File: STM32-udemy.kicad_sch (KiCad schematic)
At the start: 23 parts, among them J1 USB_B_Micro, J2 Serial_Wire, J3 Conn_01x20_Male, J4 Conn_01x20_Male, SW1 SW_Push, SW2 SW_SPDT, U1 STM32F446RCTx, Y1 Crystal_GND24

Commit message: Schematic and basic layout
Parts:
- removed C7: 100n, symbol Device:C
- added C1, C2: 10u, Capacitor_SMD:C_0805_2012Metric_Pad1.18x1.45mm_HandSolder, symbol Device:C
- added D1: PWR_LED, LED_SMD:LED_0603_1608Metric_Pad1.05x0.95mm_HandSolder, symbol Device:LED
- added H1: MountingHole, MountingHole:MountingHole_2.2mm_M2_ISO7380_Pad, symbol Mechanical:MountingHole_Pad
- added H2, H3, H4: MountingHole, MountingHole:MountingHole_2.2mm_M2_Pad, symbol Mechanical:MountingHole_Pad
- added R2: 10k, Resistor_SMD:R_0603_1608Metric_Pad0.98x0.95mm_HandSolder, symbol Device:R
- added U1: NCP1117, Package_TO_SOT_SMD:SOT-223-3_TabPin2, symbol Regulator_Linear:NCP1117-3.3_SOT223
- C10: renamed from C9; footprint (none) -> Capacitor_SMD:C_0603_1608Metric_Pad1.08x0.95mm_HandSolder
- C11: renamed from C10; footprint (none) -> Capacitor_SMD:C_0603_1608Metric_Pad1.08x0.95mm_HandSolder
- C12: renamed from C11; footprint (none) -> Capacitor_SMD:C_0603_1608Metric_Pad1.08x0.95mm_HandSolder
- C13: renamed from C12; footprint (none) -> Capacitor_SMD:C_0402_1005Metric_Pad0.74x0.62mm_HandSolder
- C14: renamed from C13; footprint (none) -> Capacitor_SMD:C_0402_1005Metric_Pad0.74x0.62mm_HandSolder
- C3: renamed from C1; footprint (none) -> Capacitor_SMD:C_0805_2012Metric_Pad1.18x1.45mm_HandSolder
- C4: renamed from C2; footprint (none) -> Capacitor_SMD:C_0603_1608Metric_Pad1.08x0.95mm_HandSolder
- C5: renamed from C3; footprint (none) -> Capacitor_SMD:C_0603_1608Metric_Pad1.08x0.95mm_HandSolder
- C6: renamed from C4; footprint (none) -> Capacitor_SMD:C_0603_1608Metric_Pad1.08x0.95mm_HandSolder
- C7: renamed from C5; footprint (none) -> Capacitor_SMD:C_0603_1608Metric_Pad1.08x0.95mm_HandSolder
- C8: renamed from C6; footprint (none) -> Capacitor_SMD:C_0603_1608Metric_Pad1.08x0.95mm_HandSolder
- C9: renamed from C8; footprint (none) -> Capacitor_SMD:C_0603_1608Metric_Pad1.08x0.95mm_HandSolder
- FB1: footprint (none) -> Inductor_SMD:L_0603_1608Metric_Pad1.05x0.95mm_HandSolder
- J1: footprint (none) -> Connector_USB:USB_Micro-B_Wuerth_629105150521
- J2: footprint (none) -> Connector_PinHeader_2.54mm:PinHeader_1x04_P2.54mm_Vertical
- J3, J4: footprint (none) -> Connector_PinHeader_2.54mm:PinHeader_1x20_P2.54mm_Vertical
- R1: value 10k -> 1K; footprint (none) -> Resistor_SMD:R_0603_1608Metric_Pad0.98x0.95mm_HandSolder
- SW1: footprint (none) -> Button_Switch_SMD:SW_Push_1P1T_NO_Vertical_Wuerth_434133025816
- SW2: footprint (none) -> Button_Switch_SMD:SW_SPDT_PCM12
- Y1: footprint (none) -> Crystal:Crystal_SMD_3225-4Pin_3.2x2.5mm
- renumbered U1 to U2
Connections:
- net +3V3: now also J2.1 (Pin_1), C2.1, D1.2 (A), U1.2 (VO); no longer J2.4 (Pin_4)
- net BOOT0: now also R2.1; no longer R1.1
- net GND: now also R1.2, C1.2, C2.2, H1.1, H2.1, H3.1, H4.1, U1.1 (GND)
- net SWCLK: now also J2.4 (Pin_4); no longer J2.3 (Pin_3)
- net SWDIO: now also J2.3 (Pin_3); no longer J2.1 (Pin_1)
- net SW_BOOT0: now also R2.2; no longer R1.2
- net VBUS: now also C1.1, U1.3 (VI); no longer U2.42 (PA9)
- net HSE_IN: now reaches C13.1, U2.5 (PH0), Y1.1
- net HSE_OUT: now reaches C14.1, U2.6 (PH1), Y1.3
- net PC0: no longer names the net of U2.8 (PC0)
- net PC1: no longer names the net of U2.9 (PC1)
- net PC2: no longer names the net of U2.10 (PC2)
- net PC3: no longer names the net of U2.11 (PC3)
- net USB_ID: no longer names the net of U2.43 (PA10)
- net USB_ID: no longer J1.4 (ID)
- new net PWR_LED: D1.1 (K), R1.1
- no-connect marks 2 -> 7
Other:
- note added: "Analog Supply filtering"
- note added: "BOOT selector switch"
- note added: "Connectors"
- note added: "Crystal oscillator circuitry"
- note added: "Decoupling capacitors"
- note added: "LED to indicate when the board is powered ON"
- note added: "Linear voltage regulator to power the board from the USB (nominal 5V)"
- note added: "Microcontroller circuitry"
- note added: "Mounting Holes"
- note added: "One 10uF Cap for the whole IC and one 100nF Cap for each VDD/VBAT pin - AN4488"
- note added: "Power LED"
- note added: "Power Supply"
- note added: "Reset Button"
- note added: "SIZE: M2"
- note added: "Serial Wire Debbuger/Programmer"
- note added: "This sequence is the same of STLink we use, wich helps with wiring"
- note added: "USB port - type B"
- note removed: "This sequence is the same of STLink V2, wich helps with wiring"
- title: (none) -> RedPill
- moved on the sheet: C10, C11, C12, C13, C14, C3, C4, C5, C6, C7, C8, C9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

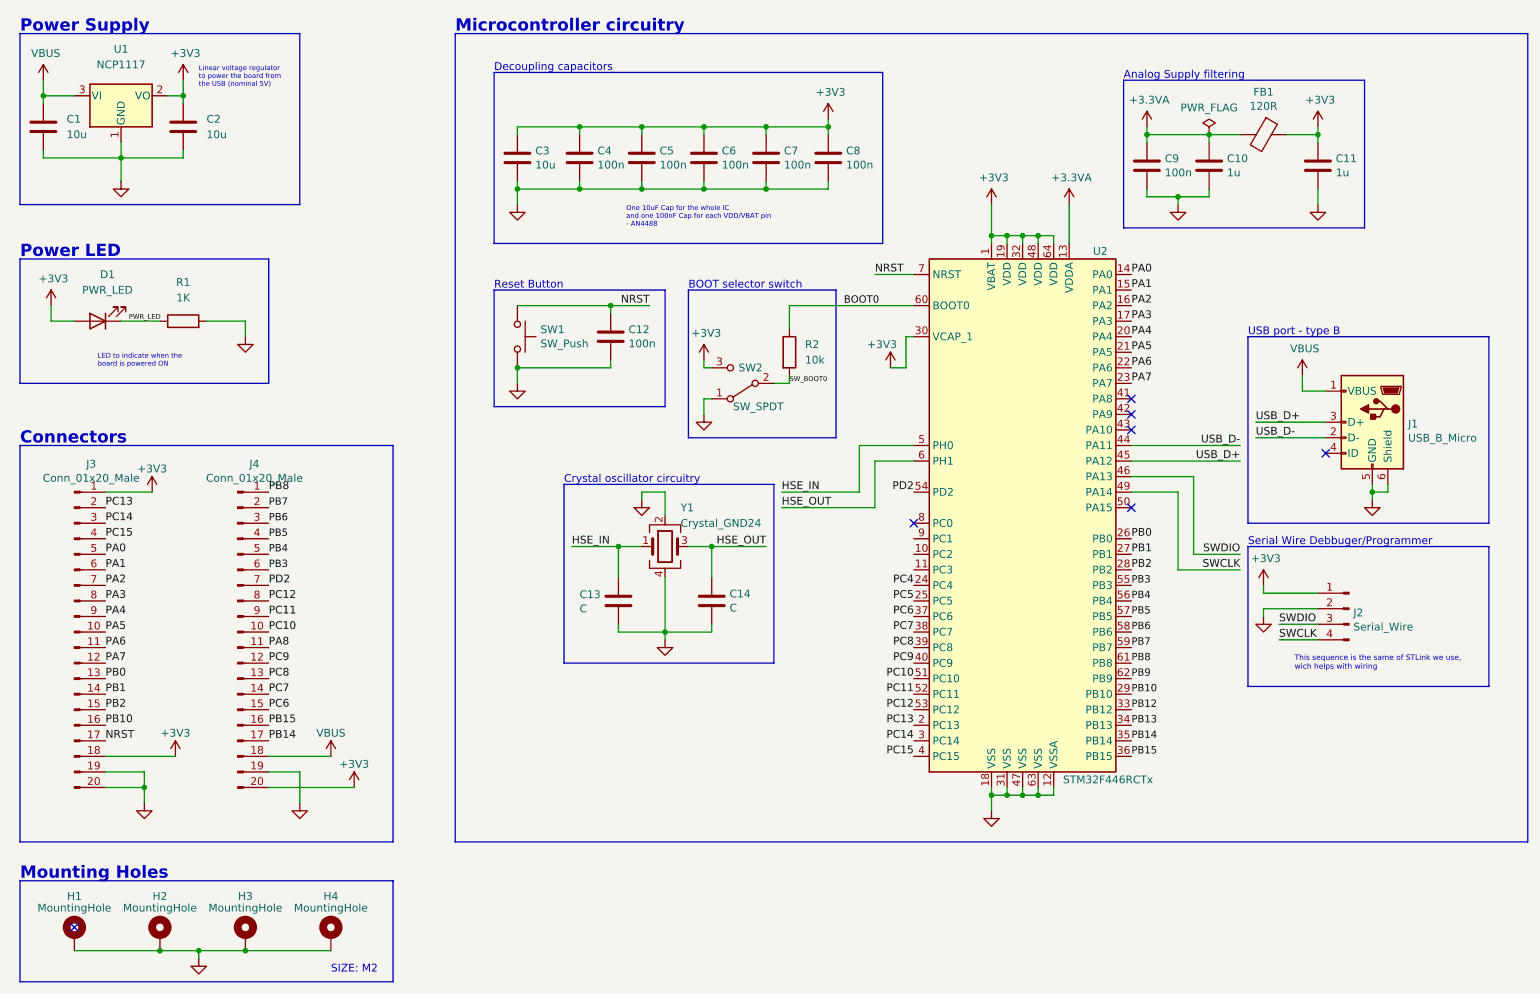
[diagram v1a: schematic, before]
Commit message: Remove components that are not essential
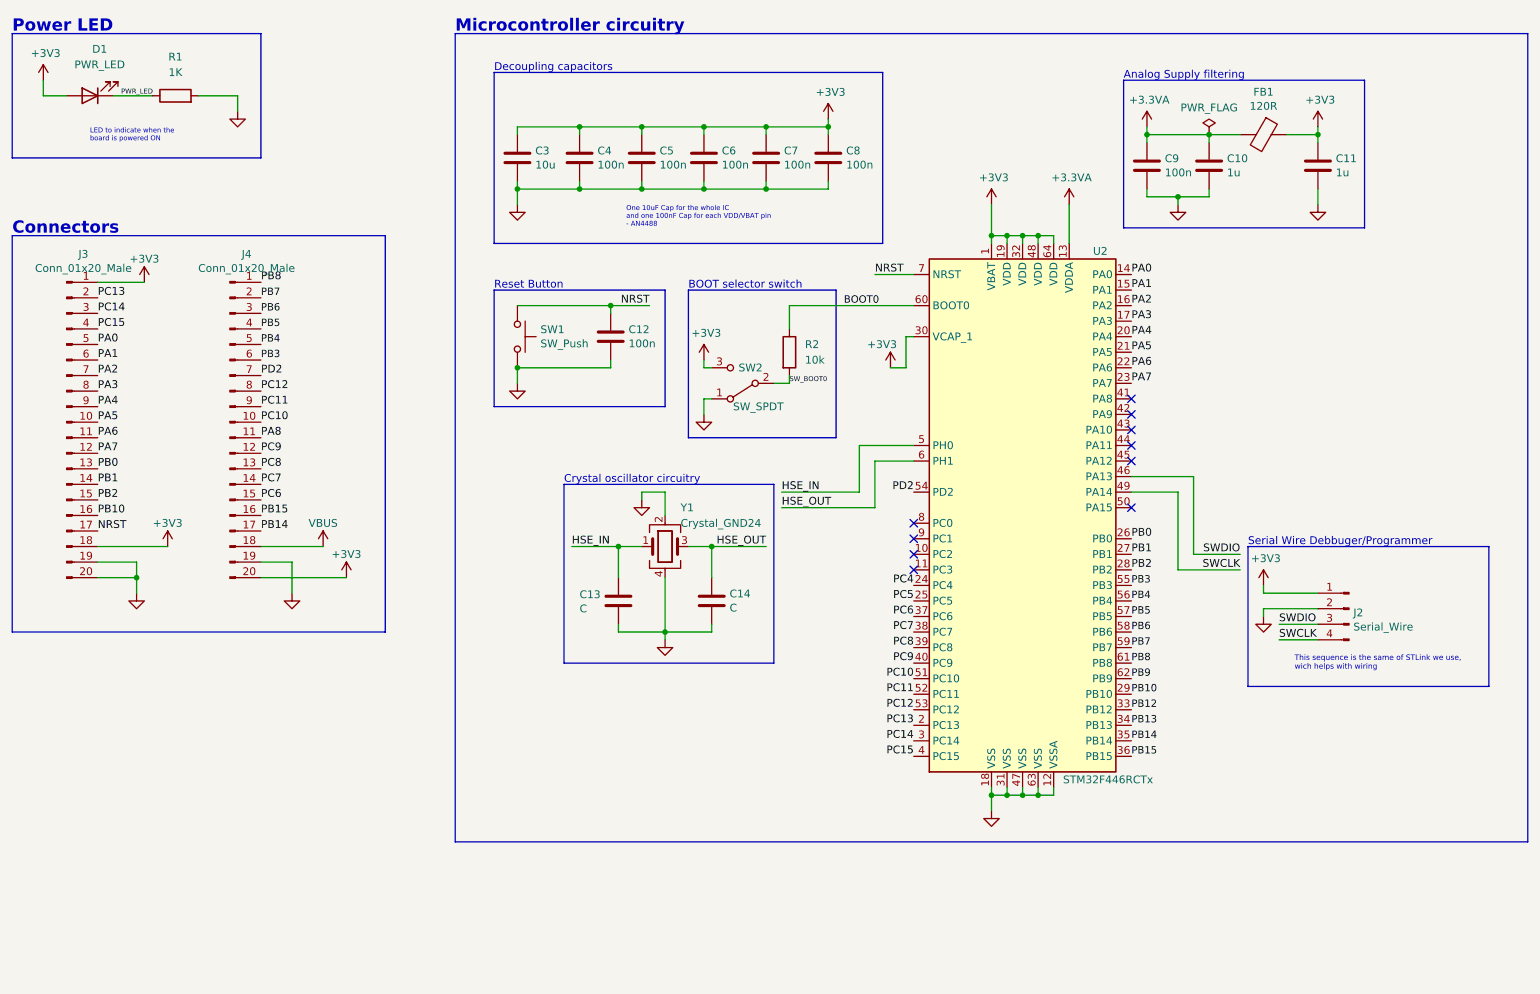
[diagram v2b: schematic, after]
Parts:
- removed C1, C2: 10u, Capacitor_SMD:C_0805_2012Metric_Pad1.18x1.45mm_HandSolder, symbol Device:C
- removed H1: MountingHole, MountingHole:MountingHole_2.2mm_M2_ISO7380_Pad, symbol Mechanical:MountingHole_Pad
- removed H2, H3, H4: MountingHole, MountingHole:MountingHole_2.2mm_M2_Pad, symbol Mechanical:MountingHole_Pad
- removed J1: USB_B_Micro, Connector_USB:USB_Micro-B_Wuerth_629105150521, symbol Connector:USB_B_Micro
- removed U1: NCP1117, Package_TO_SOT_SMD:SOT-223-3_TabPin2, symbol Regulator_Linear:NCP1117-3.3_SOT223
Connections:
- net USB_D+: no longer names the net of U2.45 (PA12)
- net USB_D-: no longer names the net of U2.44 (PA11)
- no-connect marks 7 -> 10
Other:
- note removed: "Linear voltage regulator to power the board from the USB (nominal 5V)"
- note removed: "Mounting Holes"
- note removed: "Power Supply"
- note removed: "SIZE: M2"
- note removed: "USB port - type B"
- moved on the sheet: D1, J3, J4, R1

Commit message: Initial board layout
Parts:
- renumbered C3 to C1, C12 to C10, C13 to C11, C14 to C12, C4 to C2, C5 to C3, C6 to C4, C7 to C5, C8 to C6, C9 to C7, C10 to C8, C11 to C9, J3 to J1, J4 to J2, J2 to J3, U2 to U1
